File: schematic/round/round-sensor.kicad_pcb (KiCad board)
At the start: 2 copper layers, 30 x 30 mm, 31 parts, among them P1 BUS, P2 BUS, P3 SWD, P4 PA0, P5 PA1, P6 PA3, P7 PA10, P8 V+, P9 V-, Q1 Q_NMOS_GSD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

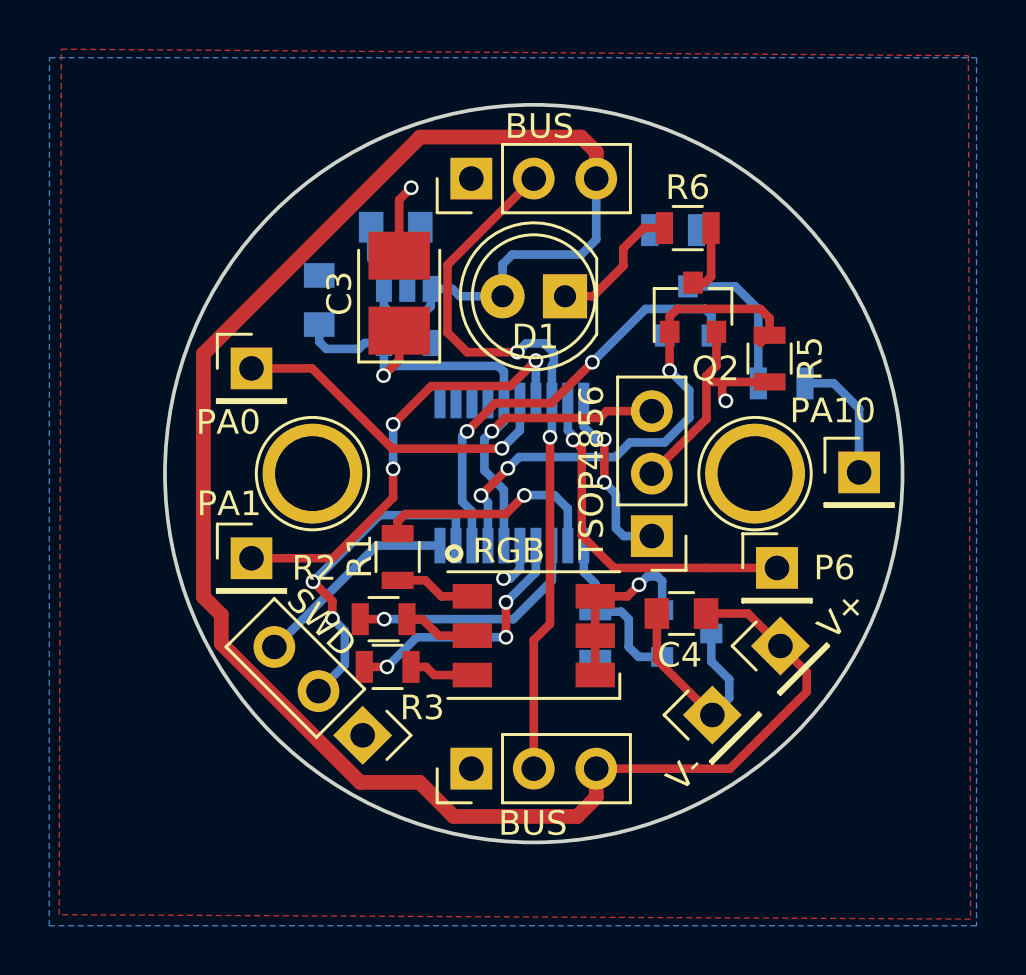
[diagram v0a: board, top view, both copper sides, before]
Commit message: Round sensor fixed for plexiglass box
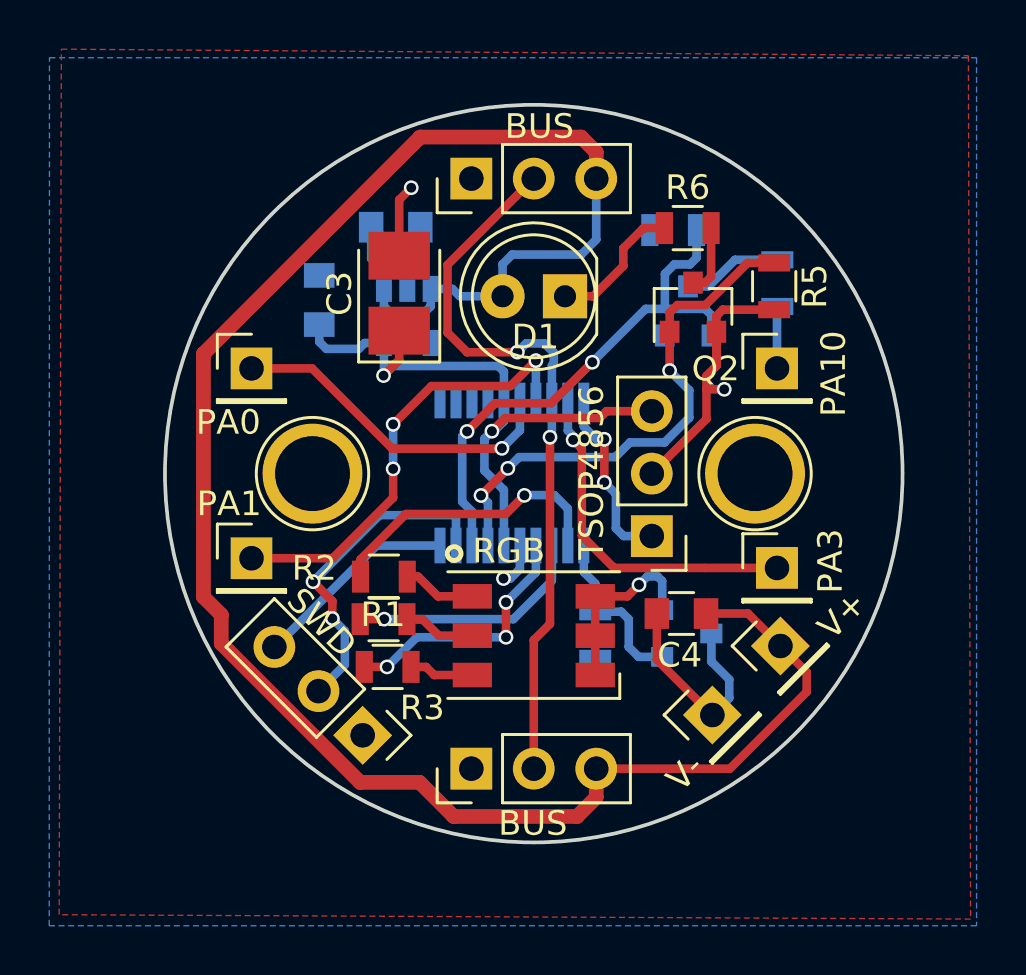
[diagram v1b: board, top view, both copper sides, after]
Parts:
- moved P7 5.39 mm to (9.89, -4.28)
- moved R8 4.08 mm to (9.91, -7.75), turned to 90 degrees
- moved R5 2.95 mm to (9.78, -7.62)
- moved R1 0.98 mm to (-6.10, 4.19), turned to 180 degrees
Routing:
- net PA10: track 17.8 -> 21.9 mm
- net Net-(P7-Pad1): track 5.22 -> 2.52 mm
- net red: track 9.59 -> 11.9 mm
- net Net-(Q3-Pad3): track 6.26 -> 4.08 mm
- net GND: track 22.2 -> 23.9 mm
